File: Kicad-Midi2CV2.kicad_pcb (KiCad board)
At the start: 2 copper layers, 99.7 x 99.7 mm, 87 parts, among them IC1 MCP4725module, IC2 MCP4725module, J1 Doepfer connector, J10 CV4, J11 Gate1, J12 GateConn, J13 Gate2, J14 Gate3, J15 Gate4, J16 I2C_Conn, J17 I2C_Conn, J18 GateConn, J19 CV7 in, J2 Vin 7-12v, J20 CV3 in, J3 MIDI OUT, J4 CV6 in, J5 Power Conn, J6 CV1, J7 CV2, J8 MIDI IN, J9 CV3, Q1 MMBT2222A, Q2 MMBT2222A, SW1 KY40_Rotary_Encoder_Module, U1 TL072, U2 EL814, U3 MCP4728

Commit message: Initial PCB Layout MK2 - incomplete
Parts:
- removed D1: LED1, LED_THT:LED_D3.0mm_Horizontal_O6.35mm_Z6.0mm
- removed D2: LED2, LED_THT:LED_D3.0mm_Horizontal_O6.35mm_Z6.0mm
- removed D3: LED3, LED_THT:LED_D3.0mm_Horizontal_O6.35mm_Z6.0mm
- removed D4: LED4, LED_THT:LED_D3.0mm_Horizontal_O6.35mm_Z6.0mm
- removed D5: LEDset1, LED_THT:LED_D3.0mm_Horizontal_O6.35mm_Z6.0mm
- removed D6: LEDset2, LED_THT:LED_D3.0mm_Horizontal_O6.35mm_Z6.0mm
- removed J10: CV4, Connector_Audio:AudioJack3StereoNarrow-PJ-321
- removed J11: Gate1, Connector_Audio:AudioJack3StereoNarrow-PJ-321
- removed J12, J18: GateConn, Connector_PinSocket_2.54mm:PinSocket_1x06_P2.54mm_Vertical
- removed J13: Gate2, Connector_Audio:AudioJack3StereoNarrow-PJ-321
- removed J16, J17: I2C_Conn, Connector_PinSocket_2.54mm:PinSocket_1x06_P2.54mm_Vertical
- removed J5: Power Conn, Connector_PinHeader_2.54mm:PinHeader_1x04_P2.54mm_Vertical
- removed J6: CV1, Connector_Audio:AudioJack3StereoNarrow-PJ-321
- removed J7: CV2, Connector_Audio:AudioJack3StereoNarrow-PJ-321
- removed J9: CV3, Connector_Audio:AudioJack3StereoNarrow-PJ-321
- removed R16, R17: 0R, Resistor_SMD:R_0805_2012Metric_Pad1.15x1.40mm_HandSolder
- removed REF** (x2): M2_MCP4725, MountingHole:MountingHole_2.2mm_M2_Pad_Via
- removed REF** (x6): Mounting_3.2mm, MountingHole:MountingHole_3.2mm_M3_Pad_Via
- removed U3: MCP4728, Package_SO:MSOP-10_3x3mm_P0.5mm
- added C103: 100n, Capacitor_SMD:C_0805_2012Metric_Pad1.15x1.40mm_HandSolder, F.Cu at (245.8, 86.0)
- added C105: 100uF, Capacitor_THT:CP_Radial_D5.0mm_P2.50mm, F.Cu at (228.0, 87.8)
- added C108: 100n, Capacitor_SMD:C_0805_2012Metric_Pad1.15x1.40mm_HandSolder, F.Cu at (227.0, 96.1)
- added C109: 100n, Capacitor_SMD:C_0805_2012Metric_Pad1.15x1.40mm_HandSolder, F.Cu at (230.8, 96.1)
- added C112: 100n, Capacitor_SMD:C_0805_2012Metric_Pad1.15x1.40mm_HandSolder, F.Cu at (234.5, 90.5)
- added C113: 100n, Capacitor_SMD:C_0805_2012Metric_Pad1.15x1.40mm_HandSolder, F.Cu at (238.3, 90.5)
- added D101: 1N1007, Diode_SMD:D_SOD-123, F.Cu at (219.0, 92.9)
- added D102: 1N1007, Diode_SMD:D_SOD-123, F.Cu at (223.8, 92.9)
- added D103: 1N4148W, Diode_SMD:D_SOD-123, F.Cu at (219.0, 95.3)
- added D104: LED1, LED_THT:LED_D3.0mm, F.Cu at (194.0, -3.99)
- added D105: LED2, LED_THT:LED_D3.0mm, F.Cu at (194.0, -9.08)
- added D106: LED3, LED_THT:LED_D3.0mm, F.Cu at (194.0, -14.2)
- added D107: LED4, LED_THT:LED_D3.0mm, F.Cu at (194.0, -19.2)
- added D108: LED MIDI, LED_THT:LED_D3.0mm, F.Cu at (194.0, -26.9)
- added D109: LED LFO, LED_THT:LED_D3.0mm, F.Cu at (233.2, 87.3)
- added D110: LED CV1, LED_THT:LED_D3.0mm, F.Cu at (194.0, -31.9)
- added D111: LED CV2, LED_THT:LED_D3.0mm, F.Cu at (227.5, 92.8)
- added F101: Polyfuse, Fuse:Fuse_1206_3216Metric_Pad1.42x1.75mm_HandSolder, F.Cu at (215.5, 117.7)
- added J104: Power Conn, Connector_PinHeader_2.54mm:PinHeader_1x06_P2.54mm_Vertical, F.Cu at (140.7, -26.6)
- added J106: Gate1, AJ-Dropbox-Kicad:PJ301SM, F.Cu at (103.1, 1.09)
- added J109: Gate2, AJ-Dropbox-Kicad:PJ301SM, F.Cu at (103.1, 9.98)
- added J112: CV1, AJ-Dropbox-Kicad:PJ301SM, F.Cu at (103.1, -54.2)
- added J114: CV2, AJ-Dropbox-Kicad:PJ301SM, F.Cu at (103.1, -45.3)
- added J115: ControlConn, Connector_PinHeader_2.54mm:PinHeader_1x12_P2.54mm_Vertical, F.Cu at (214.8, 86.8)
- added J116: ControlConn, Connector_PinHeader_2.54mm:PinHeader_1x12_P2.54mm_Horizontal, F.Cu at (164.1, -9.07)
- added J117: I2C_Conn, Connector_PinHeader_2.54mm:PinHeader_1x08_P2.54mm_Vertical, F.Cu at (130.4, -28.1)
- added J118: I2C_Conn, Connector_PinHeader_2.54mm:PinHeader_1x08_P2.54mm_Horizontal, F.Cu at (164.1, -28.1)
- added JP101: GND MIDI OUT, Jumper:SolderJumper-2_P1.3mm_Bridged_RoundedPad1.0x1.5mm, F.Cu at (230.2, 98.3)
- added JP104: GND MIDI OUT, Jumper:SolderJumper-2_P1.3mm_Open_RoundedPad1.0x1.5mm, F.Cu at (226.8, 98.6)
- added R101: 1k, Resistor_SMD:R_0805_2012Metric_Pad1.15x1.40mm_HandSolder, F.Cu at (223.3, 97.0)
- added R108: OPEN, Resistor_SMD:R_0805_2012Metric_Pad1.15x1.40mm_HandSolder, F.Cu at (238.8, 87.9)
- added R110: OPEN, Resistor_SMD:R_0805_2012Metric_Pad1.15x1.40mm_HandSolder, F.Cu at (242.5, 87.9)
- added R112: OPEN, Resistor_SMD:R_0805_2012Metric_Pad1.15x1.40mm_HandSolder, F.Cu at (246.3, 87.9)
- added R113: 220R, Resistor_SMD:R_0805_2012Metric_Pad1.15x1.40mm_HandSolder, F.Cu at (242.0, 89.9)
- added R116: OPEN, Resistor_SMD:R_0805_2012Metric_Pad1.15x1.40mm_HandSolder, F.Cu at (242.0, 91.8)
- added R117: 2k, Resistor_SMD:R_0805_2012Metric_Pad1.15x1.40mm_HandSolder, F.Cu at (233.1, 92.5)
- added R119: OPEN, Resistor_SMD:R_0805_2012Metric_Pad1.15x1.40mm_HandSolder, F.Cu at (236.9, 92.5)
- added R121: 10k, Resistor_SMD:R_0805_2012Metric_Pad1.15x1.40mm_HandSolder, F.Cu at (234.5, 94.4)
- added R122: 10k, Resistor_SMD:R_0805_2012Metric_Pad1.15x1.40mm_HandSolder, F.Cu at (238.3, 94.4)
- added R131: 10k, Resistor_SMD:R_0805_2012Metric_Pad1.15x1.40mm_HandSolder, F.Cu at (234.5, 96.4)
- added R132: 10k, Resistor_SMD:R_0805_2012Metric_Pad1.15x1.40mm_HandSolder, F.Cu at (223.3, 95.1)
- added R138: 680R, Resistor_SMD:R_0805_2012Metric_Pad1.15x1.40mm_HandSolder, F.Cu at (238.3, 96.4)
- added R140: 680R, Resistor_SMD:R_0805_2012Metric_Pad1.15x1.40mm_HandSolder, F.Cu at (242.0, 86.0)
- added U102: TL072, AJ-Dropbox-Kicad:AJ_SO-8_5.3x6.2mm_P1.27mm, F.Cu at (221.5, 88.4)
- R111: renamed from R6; value 1k -> OPEN
- R118: renamed from R9; value 1k -> OPEN
- moved J102 157.5 mm to (155.3, -26.0)
- moved C102 110.6 mm to (141.3, -0.18)
- moved J103 110.6 mm to (188.2, 30.3)
- moved J107 110.6 mm to (188.2, 9.98)
- moved Q101 110.6 mm to (172.3, 27.8)
- moved R129 110.6 mm to (148.5, -19.2)
- moved R130 110.6 mm to (141.3, -19.2)
- moved R141 110.6 mm to (186.3, -51.6)
- moved U103 110.6 mm to (174.2, 11.9)
- moved A101 110.6 mm to (160.1, 1.09)
- moved C101 110.6 mm to (153.3, 22.7)
- moved C104 110.6 mm to (111.4, -14.9)
- moved C106 110.6 mm to (128.5, -33.8)
- moved C107 110.6 mm to (117.7, -29.9)
- moved C110 110.6 mm to (131.1, -44.0)
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- renumbered A1 to A101, C1 to C101, C2 to C102, C3 to C104, C4 to C106, C5 to C107, C6 to C110, C7 to C111, C8 to C114, C9 to C115, C10 to C116, C11 to C117, IC1 to IC101, IC2 to IC102, J1 to J101, J2 to J102, J3 to J103, J19 to J105, J8 to J107, J4 to J108, J20 to J110, J14 to J111, J15 to J113, JP1 to JP102, JP2 to JP103, Q1 to Q101, Q2 to Q102, R29 to R102, R3 to R103, R5 to R104, R2 to R105, R11 to R106, R12 to R107, R7 to R109, R4 to R114, R1 to R115, R13 to R120, R25 to R123, R14 to R124, R26 to R125, R8 to R126, R15 to R127, R10 to R128, R27 to R129, R28 to R130, R18 to R133, R19 to R134, R20 to R135, R21 to R136, R22 to R137, R23 to R139, R24 to R141, RV2 to RV101, RV1 to RV102, SW1 to SW101, U1 to U101, U2 to U103
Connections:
- net /-12v renamed -12V
- net /12v renamed +12V
- net /SCL renamed SCL
- net /SDA renamed SDA
- net LED-sel renamed LED-MIDI
- net LED-sel2 renamed LED-CV1
- net Net-(JP2-Pad1) renamed /Q2Coll
- A101 pad 15: /RDY-BSY -> LED-CV2
- A101 pad 16: /LDAC -> LED_LFO
- A101 pad 17: Net-(A1-Pad17) -> Net-(A101-Pad17)
- C114 pad 2: Net-(A1-Pad17) -> +5V
- IC101 pad 1: /Vout1 -> CV1
- IC102 pad 1: /Vout2 -> CV2
- J102 pad 1: VCC -> Net-(F101-Pad2)
- J103 pad 2: (no net) -> Net-(J103-Pad2)
- J103 pad 4: Net-(J3-Pad4) -> /MIDI-OUT-4
- J103 pad 5: GND -> /MIDI-OUT-5
- J105 pad S: GND -> Net-(J105-PadS)
- J107 pad 2: (no net) -> Net-(J107-Pad2)
- J108 pad S: GND -> Net-(J105-PadS)
- J110 pad S: GND -> Net-(J105-PadS)
- J111 pad T: Gate3 -> Gate3Gain
- J113 pad T: Gate4 -> Gate4Gain
- Q101 pad 1: /TX -> /Q1Base
- Q101 pad 2: GND -> /Q1Emitter
- Q101 pad 3: /MIDI-OUT -> /Q1Coll
- R109 pad 1: /MIDI-OUT -> /MIDI-OUT-4
- R109 pad 2: Net-(J3-Pad4) -> +5V
- R111 pad 1: /MIDI-OUT -> /Q1Base
- R118 pad 2: /TX -> /Q1Base
- R125 pad 2: GND -> Net-(J105-PadS)
- R128 pad 2: GND -> Net-(J105-PadS)
- R130 pad 2: GND -> Net-(J105-PadS)
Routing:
- net +5V: track 188.6 -> 0.00 mm, vias 12 -> 0
- net GND: track 122.7 -> 0.00 mm, vias 8 -> 0
- net -12V: track 107.1 -> 0.00 mm
- net Btn: track 87.5 -> 0.00 mm
- net +12V: track 83.8 -> 0.00 mm
- net Gate4: track 82.0 -> 0.00 mm
- net Net-(A1-Pad17): track 76.7 -> 0.00 mm
- net SCL: track 75.5 -> 0.00 mm, vias 3 -> 0
- net Gate3: track 73.4 -> 0.00 mm
- net A6: track 70.1 -> 0.00 mm
- net Net-(J110-PadT): track 69.4 -> 0.00 mm, vias 4 -> 0
- net CV1: track 68.6 -> 0.00 mm, vias 4 -> 0
- net A1: track 65.4 -> 0.00 mm
- net A2: track 64.7 -> 0.00 mm
- net Gate2: track 64.0 -> 0.00 mm, vias 1 -> 0
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- removed copper zone on F.Cu, net +5V
- removed copper zone on B.Cu, net GND
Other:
- board size 99.7 x 99.7 mm -> 100 x 100 mm
- board text removed: "(125.1,25.4)"
- board text removed: "(25.4,25,4)"

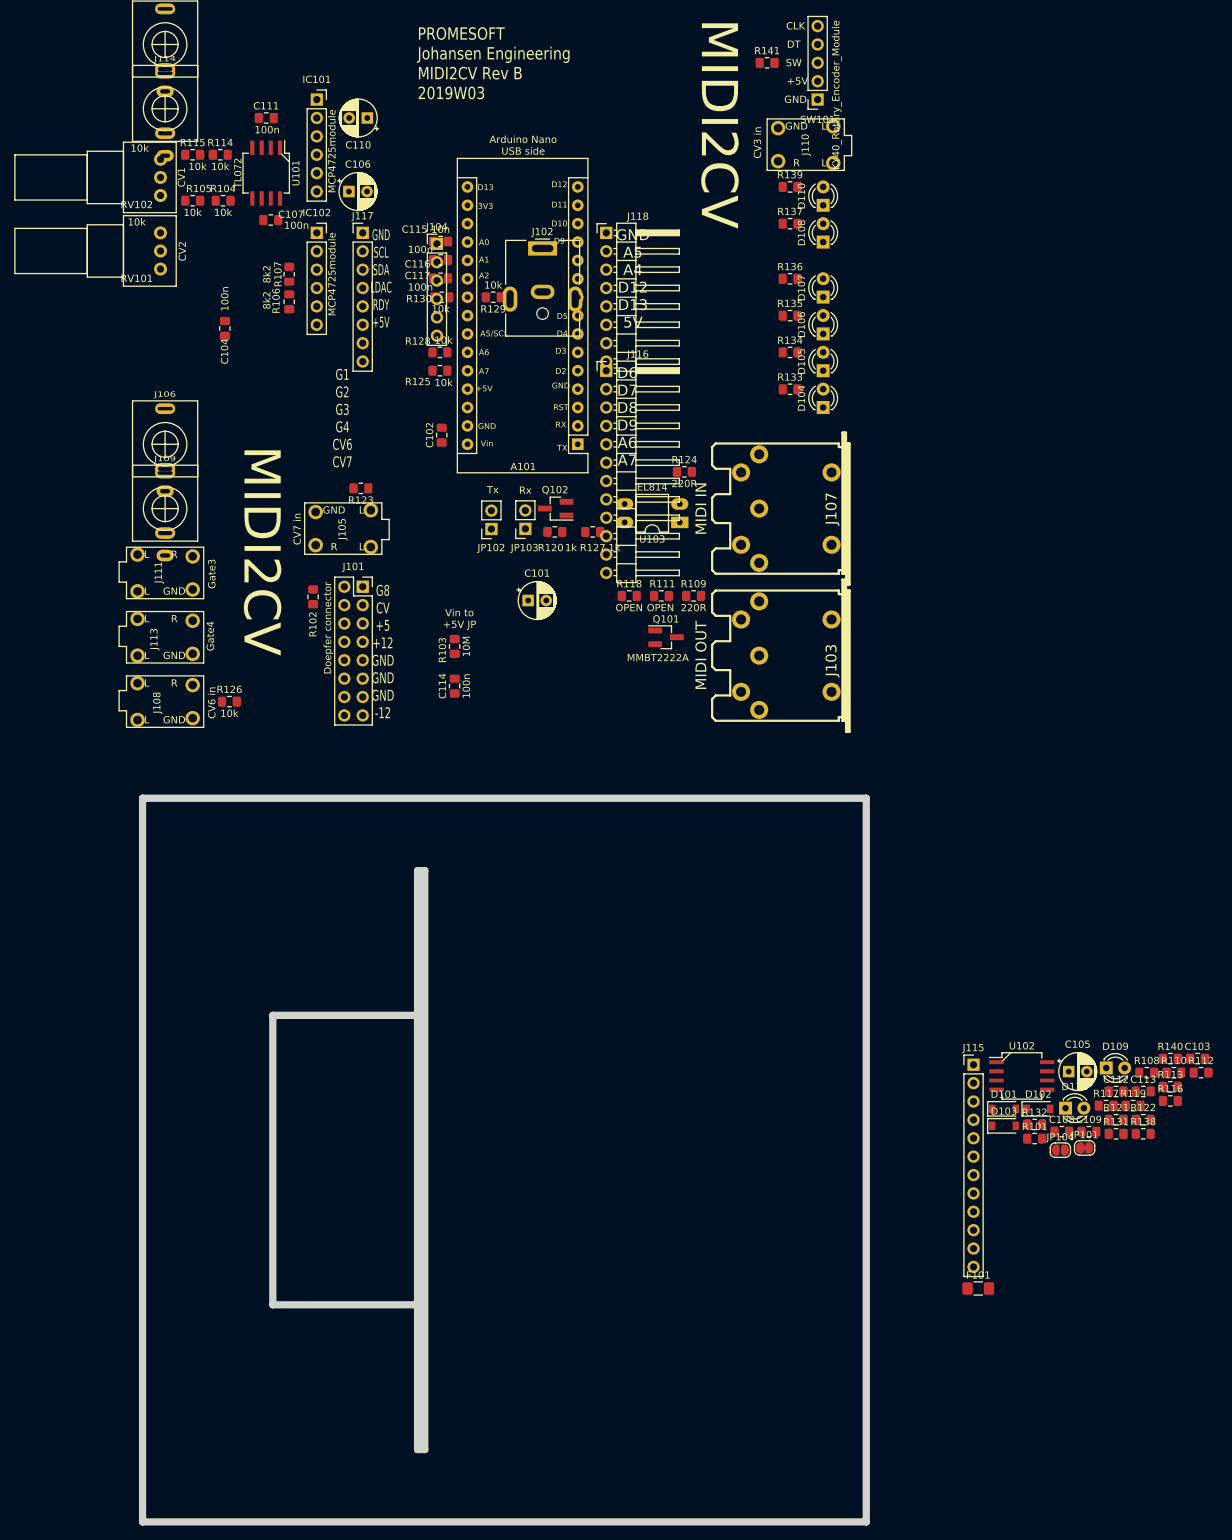
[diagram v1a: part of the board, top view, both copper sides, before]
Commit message: Footprint replace in sch, netlist and PCB
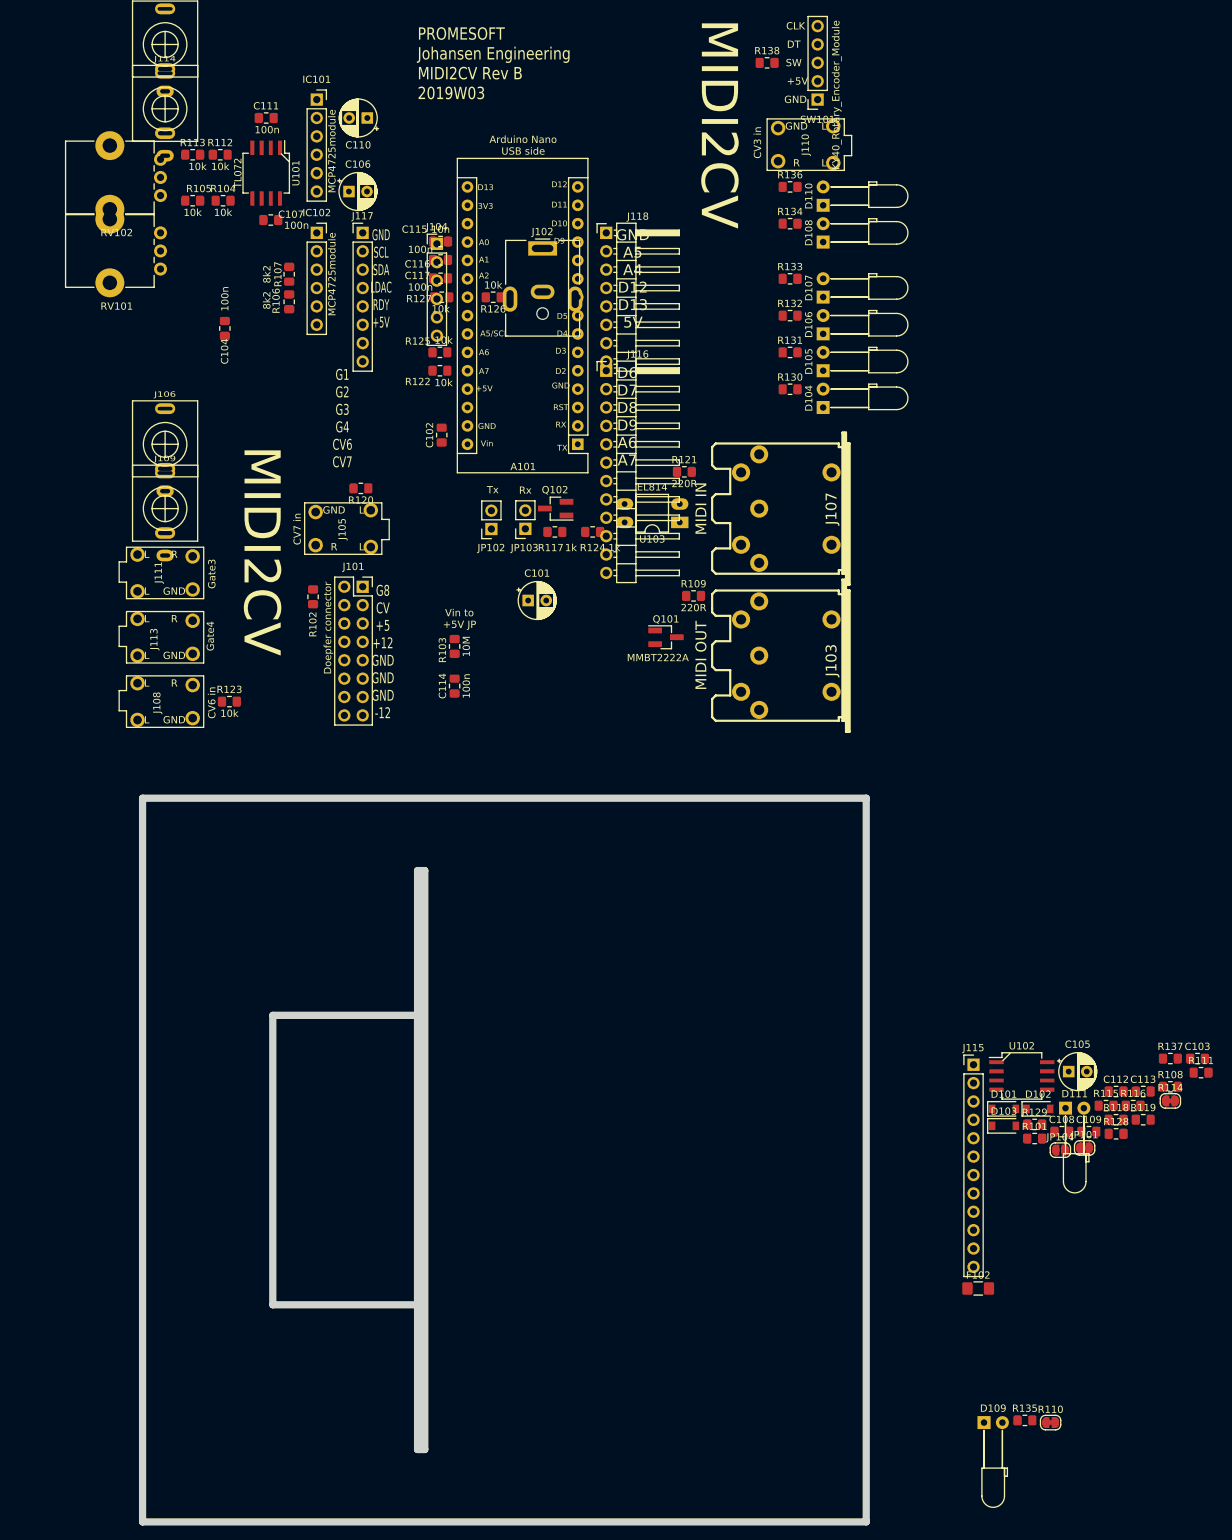
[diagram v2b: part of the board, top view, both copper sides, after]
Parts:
- removed the R108 at (238.8, 87.9)
- removed the R111 at (171.7, 22.0)
- removed the R116 at (242.0, 91.8)
- removed the R118 at (167.2, 22.0)
- removed the R138 at (238.3, 96.4)
- added R114: 0R, Jumper:SolderJumper-2_P1.3mm_Bridged_RoundedPad1.0x1.5mm, F.Cu at (242.0, 91.8)
- added R135: 680R, Resistor_SMD:R_0805_2012Metric_Pad1.15x1.40mm_HandSolder, F.Cu at (221.9, 136.0)
- D104, D105, D106, D107: footprint LED_THT:LED_D3.0mm -> LED_THT:LED_D3.0mm_Horizontal_O6.35mm_Z6.0mm
- D108: value LED MIDI -> LEDset1; footprint LED_THT:LED_D3.0mm -> LED_THT:LED_D3.0mm_Horizontal_O6.35mm_Z6.0mm
- D109: value LED LFO -> LEDset1; footprint LED_THT:LED_D3.0mm -> LED_THT:LED_D3.0mm_Horizontal_O6.35mm_Z6.0mm
- D110: value LED CV1 -> LEDset2; footprint LED_THT:LED_D3.0mm -> LED_THT:LED_D3.0mm_Horizontal_O6.35mm_Z6.0mm
- D111: value LED CV2 -> LEDset2; footprint LED_THT:LED_D3.0mm -> LED_THT:LED_D3.0mm_Horizontal_O6.35mm_Z6.0mm
- R108: renamed from R113; value 220R -> OPEN
- R110: value OPEN -> 0R; footprint Resistor_SMD:R_0805_2012Metric_Pad1.15x1.40mm_HandSolder -> Jumper:SolderJumper-2_P1.3mm_Bridged_RoundedPad1.0x1.5mm
- R116: renamed from R119; value OPEN -> 680R
- RV101, RV102: footprint Potentiometer_THT:Potentiometer_Alps_RK097_Single_Horizontal -> Potentiometer_THT:Potentiometer_Alps_RK09K_Single_Vertical
- moved D109 51.8 mm to (216.3, 136.3)
- moved R110 51.3 mm to (225.5, 136.3)
- renumbered F101 to F102, R112 to R111, R114 to R112, R115 to R113, R117 to R115, R120 to R117, R121 to R118, R122 to R119, R123 to R120, R124 to R121, R125 to R122, R126 to R123, R127 to R124, R128 to R125, R129 to R126, R130 to R127, R131 to R128, R132 to R129, R133 to R130, R134 to R131, R135 to R132, R136 to R133, R137 to R134, R139 to R136, R140 to R137, R141 to R138
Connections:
- J101 pad 5: +5V -> Net-(F101-Pad1)
- J101 pad 6: +5V -> Net-(F101-Pad1)
- R110 pad 2: /Q1Base -> +5V
- R111 pad 1: /Q1Coll -> /Q1Emitter

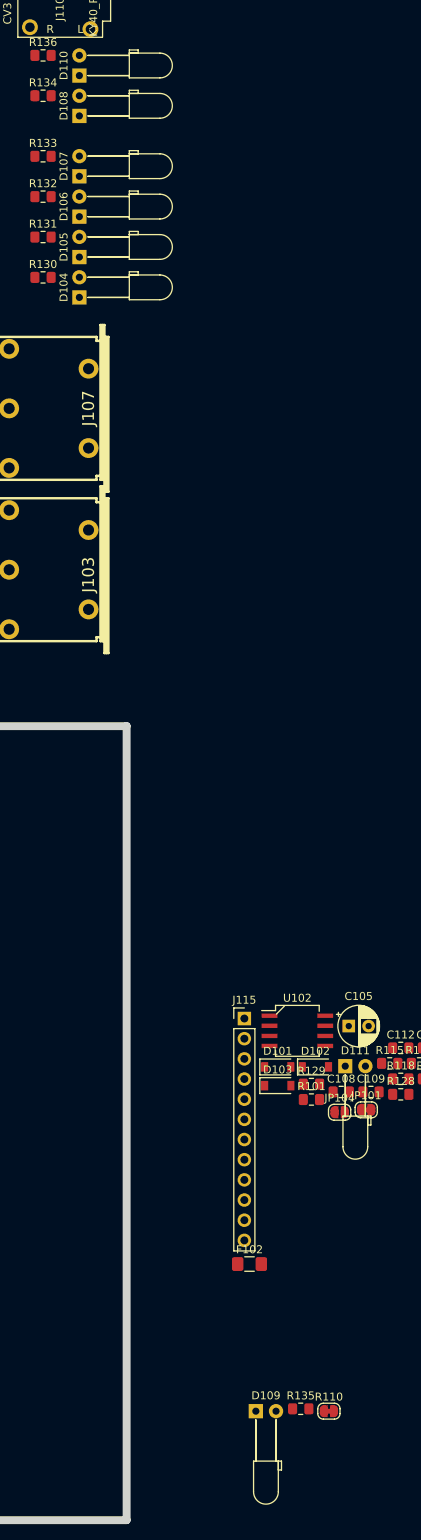
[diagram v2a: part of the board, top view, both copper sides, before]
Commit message: Footprints and LED labels
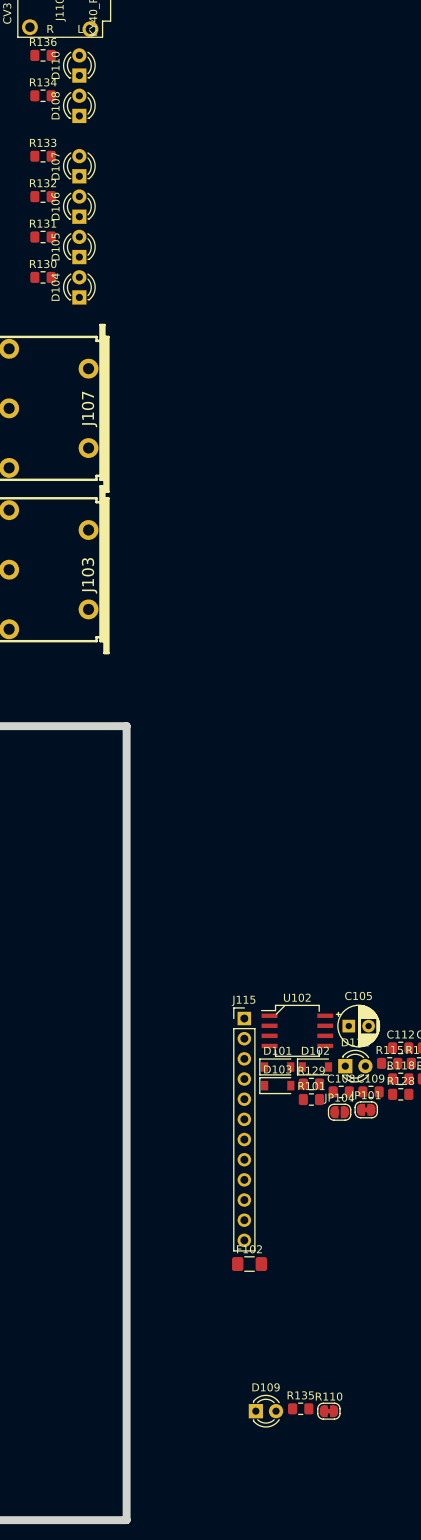
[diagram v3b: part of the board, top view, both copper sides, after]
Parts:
- D104, D105, D106, D107, D108, D109, D110, D111: footprint LED_THT:LED_D3.0mm_Horizontal_O6.35mm_Z6.0mm -> LED_THT:LED_D3.0mm
